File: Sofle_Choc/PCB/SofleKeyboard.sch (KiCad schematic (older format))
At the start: 84 parts, among them J2 4PIN, J3 OLED, P1 i2c_pin, P2 i2c_pin, SW1 SW_PUSH_LED, SW10 SW_PUSH_LED, SW11 SW_PUSH_LED, SW12 SW_PUSH_LED, SW13 SW_PUSH_LED, SW14 SW_PUSH_LED, SW15 SW_PUSH_LED, SW16 SW_PUSH_LED, SW17 SW_PUSH_LED, SW18 SW_PUSH_LED, SW19 SW_PUSH_LED, SW2 SW_PUSH_LED, SW20 SW_PUSH_LED, SW21 SW_PUSH_LED, SW22 SW_PUSH_LED, SW23 SW_PUSH_LED, SW24 SW_PUSH_LED, SW25 Rotary_Encoder_Switch, SW26 SW_PUSH_LED, SW27 SW_PUSH_LED, SW28 SW_PUSH_LED, SW29 SW_PUSH_LED, SW3 SW_PUSH_LED, SW30 SW_PUSH_LED, SW4 SW_PUSH_LED, SW5 SW_PUSH_LED, SW6 SW_PUSH_LED, SW7 SW_PUSH_LED, SW8 SW_PUSH_LED, SW9 SW_PUSH_LED, U1 ProMicro

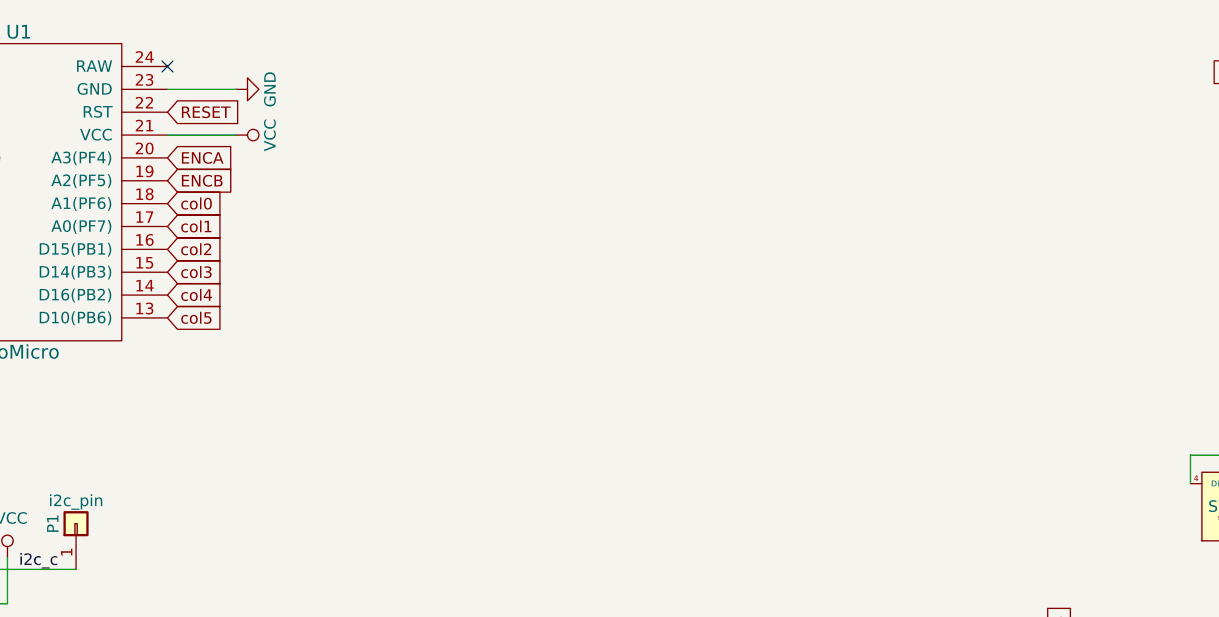
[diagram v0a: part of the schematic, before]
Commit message: Add power switch and battery tht pads to Sofle Choc
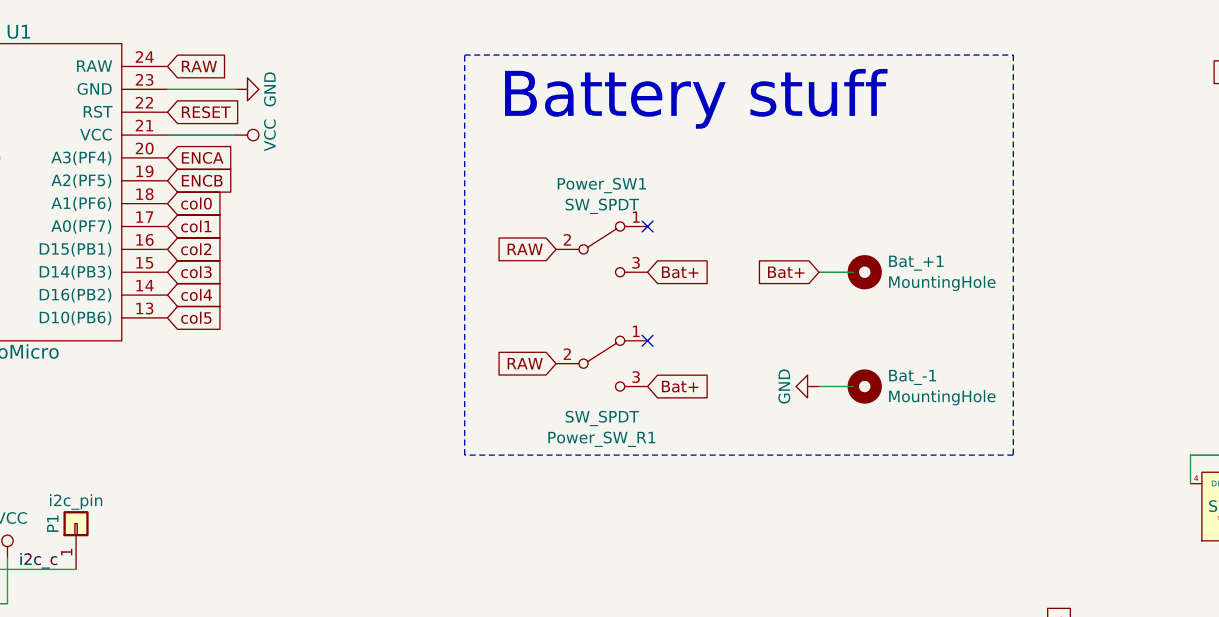
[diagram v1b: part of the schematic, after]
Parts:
- added Bat_+1, Bat_-1: MountingHole, MountingHole:MountingHole_2.1mm, symbol Mechanical:MountingHole
- added Power_SW1: SW_SPDT, SofleChoc:SPDT_C128955, symbol Switch:SW_SPDT
- added Power_SW_R1: SW_SPDT, SofleChoc:SPDT_C128955r, symbol Switch:SW_SPDT
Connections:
- net RAW: now reaches U1.24 (RAW)
- net RAW: now also Power_SW1.2 (B), Power_SW_R1.2 (B)
- new net Bat+: Power_SW1.3 (C), Power_SW_R1.3 (C)
- no-connect marks 3 -> 4
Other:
- note added: "Battery stuff"
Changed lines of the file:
@@
 Text GLabel 2400 1050 2    50   Input ~ 0
 RESET
-NoConn ~ 2400 850
 Text GLabel 1100 850  0    50   Input ~ 0
 LED
@@
 Wire Wire Line
 	10425 1200 10425 1075
+$Comp
+L Mechanical:MountingHole Bat_-1
+U 1 1 61C62848
+P 5450 2250
+F 0 "Bat_-1" H 5550 2296 50  0000 L CNN
+F 1 "MountingHole" H 5550 2205 50  0000 L CNN
+F 2 "MountingHole:MountingHole_2.1mm" H 5450 2250 50  0001 C CNN
+F 3 "~" H 5450 2250 50  0001 C CNN
+	1    5450 2250
+	1    0    0    -1
+$EndComp
+$Comp
+L SofleKeyboard-rescue:GND-Lily58-cache-Lily58_Pro-rescue #PWR0105
+U 1 1 61C71D3F
+P 5250 2250
+F 0 "#PWR0105" H 5250 2000 50  0001 C CNN
+F 1 "GND" H 5250 2100 50  0000 C CNN
+F 2 "" H 5250 2250 50  0001 C CNN
+F 3 "" H 5250 2250 50  0001 C CNN
+	1    5250 2250
+	0    1    1    0
+$EndComp
+$Comp
+L Switch:SW_SPDT Power_SW1
+U 1 1 61C5A27A
+P 4300 1650
+F 0 "Power_SW1" H 4300 1935 50  0000 C CNN
+F 1 "SW_SPDT" H 4300 1844 50  0000 C CNN
+F 2 "SofleChoc:SPDT_C128955" H 4300 1650 50  0001 C CNN
+F 3 "~" H 4300 1650 50  0001 C CNN
+	1    4300 1650
+	1    0    0    -1
+$EndComp
+Text GLabel 2400 850  2    50   Input ~ 0
+RAW
+Text GLabel 4100 1650 0    50   Input ~ 0
+RAW
+Text GLabel 4100 2150 0    50   Input ~ 0
+RAW
+NoConn ~ 4500 2050
+NoConn ~ 4500 1550
+Text GLabel 4500 1750 2    50   Input ~ 0
+Bat+
+Text GLabel 4500 2250 2    50   Input ~ 0
+Bat+
+Text GLabel 5250 1750 0    50   Input ~ 0
+Bat+
+$Comp
+L Switch:SW_SPDT Power_SW_R1
+U 1 1 61DCE246
+P 4300 2150
+F 0 "Power_SW_R1" H 4300 1825 50  0000 C CNN
+F 1 "SW_SPDT" H 4300 1916 50  0000 C CNN
+F 2 "SofleChoc:SPDT_C128955r" H 4300 2150 50  0001 C CNN
+F 3 "~" H 4300 2150 50  0001 C CNN
+	1    4300 2150
+	1    0    0    -1
+$EndComp
+Wire Wire Line
+	5250 2250 5400 2250
+Wire Notes Line
+	3700 800  6100 800
+Wire Notes Line
+	6100 800  6100 2550
+Wire Notes Line
+	6100 2550 3700 2550
+Wire Notes Line
+	3700 2550 3700 800
+Text Notes 3850 1100 0    197  ~ 0
+Battery stuff
+$Comp
+L Mechanical:MountingHole Bat_+1
+U 1 1 61C594D4
+P 5450 1750
+F 0 "Bat_+1" H 5550 1796 50  0000 L CNN
+F 1 "MountingHole" H 5550 1705 50  0000 L CNN
+F 2 "MountingHole:MountingHole_2.1mm" H 5450 1750 50  0001 C CNN
+F 3 "~" H 5450 1750 50  0001 C CNN
+	1    5450 1750
+	1    0    0    -1
+$EndComp
+Wire Wire Line
+	5250 1750 5400 1750
 $EndSCHEMATC
